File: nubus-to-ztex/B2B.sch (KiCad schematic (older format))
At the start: 13 parts, among them J1 87832-1420 (2x7 M 2mm), J3 Conn_01x06_Male

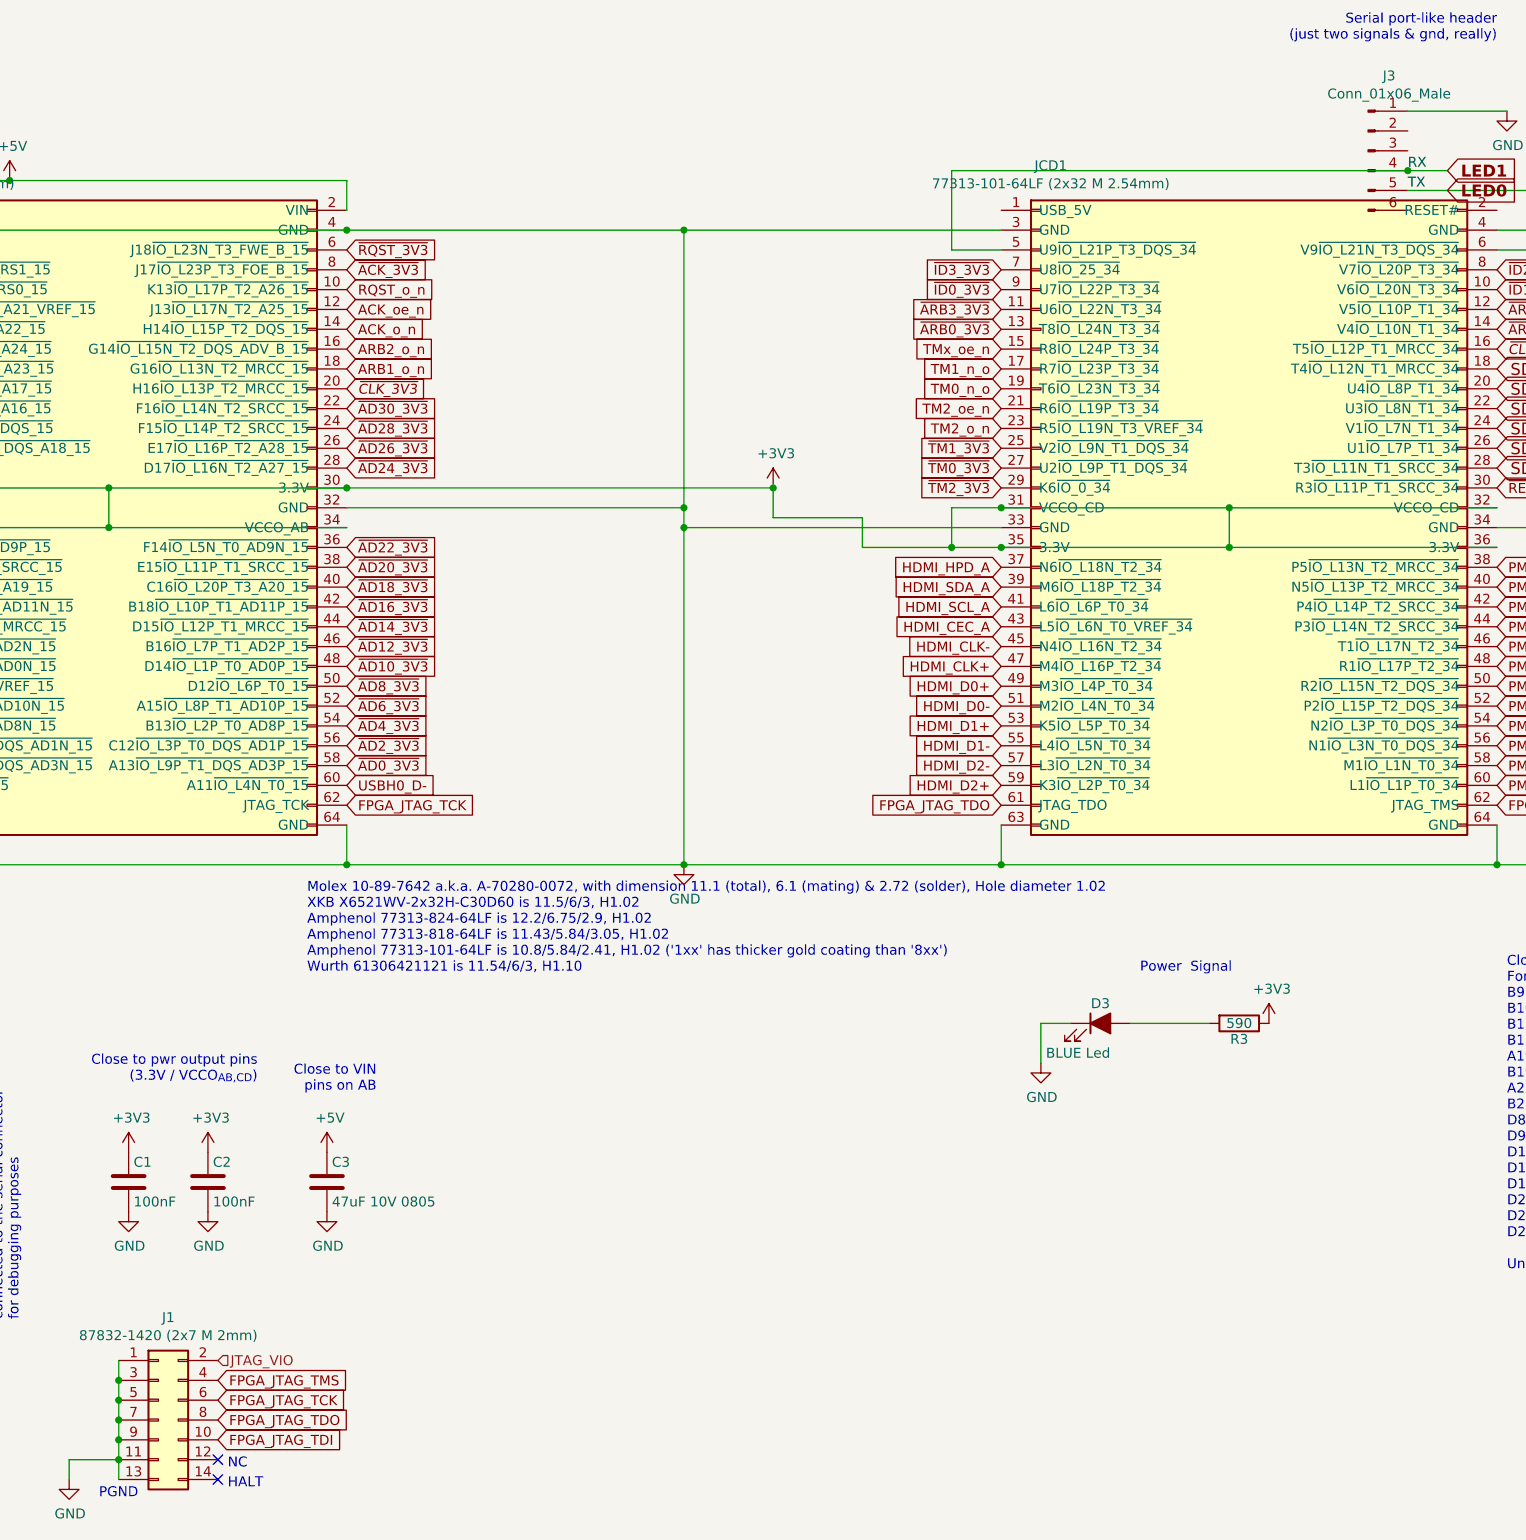
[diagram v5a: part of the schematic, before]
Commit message: more THT->SMT, lexx expensive parts/assembly (?)
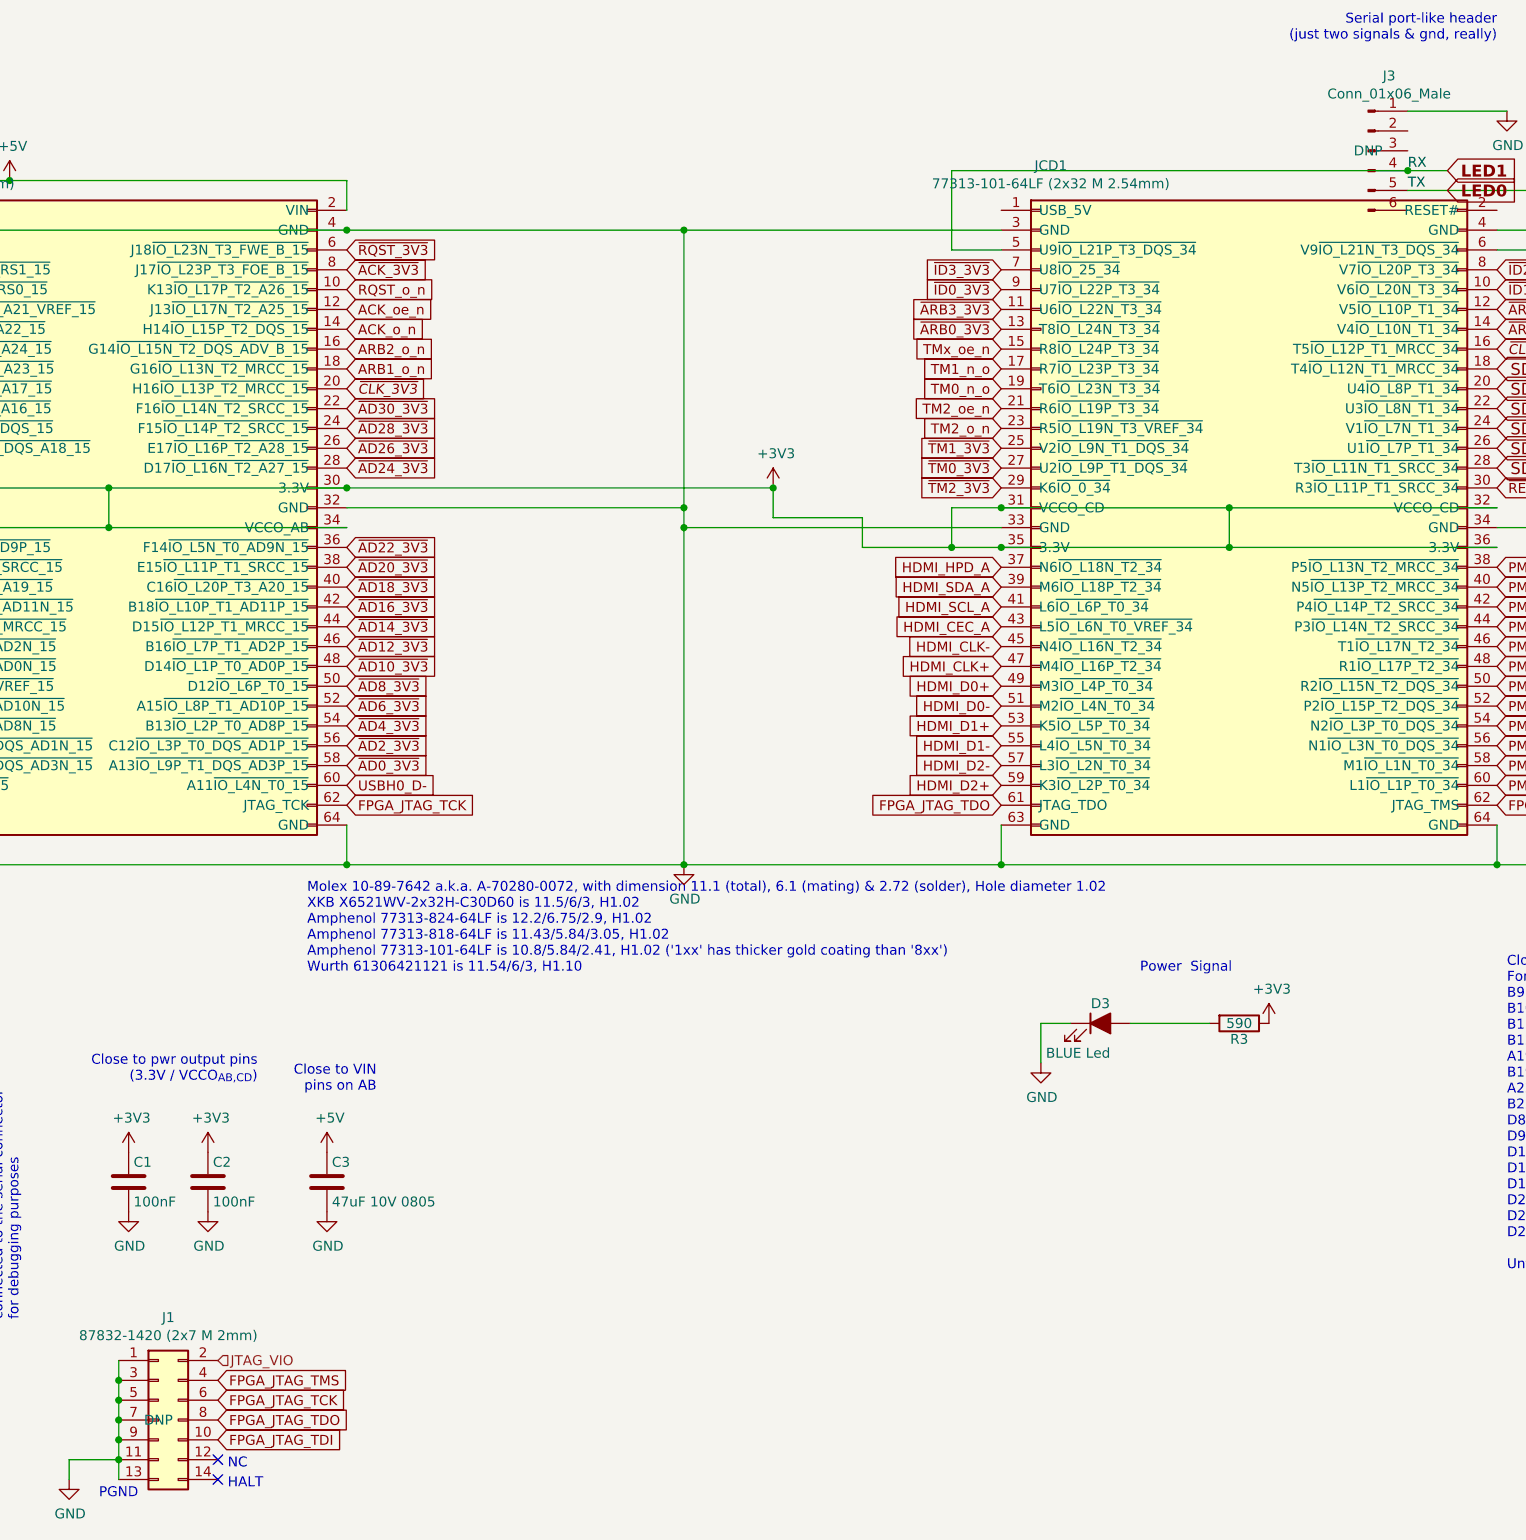
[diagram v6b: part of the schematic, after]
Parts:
- J1: DNP (none) -> DNP
- J3: footprint For_SeeedStudio:PinHeader_1x06_P2.54mm_Horizontal_For_SeeedStudio -> For_SeeedStudio:SAMTEC_TSM-106-01-L-SH; DNP (none) -> DNP; MPN PZ254R-11-06P -> TSM-106-01-T-SH; MPN comments (none) -> 'T' is tin 'L' is gold ; with extra -A (and footprint chang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; MPN-ALT 22-28-8060 -> (none); URL https://lcsc.com/product-detail/Pin-Header-Female-Header_XF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 -> https://www.mouser.fr/ProductDetail/Samtec/TSM-106-01-T-SH?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; URL-ALT https://www2.mouser.com/ProductDetail/Molex/22-28-8060?qs=4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 -> (none)
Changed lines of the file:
@@
 F 0 "J3" H 9356 1228 50  0000 C CNN
 F 1 "Conn_01x06_Male" H 9356 1137 50  0000 C CNN
-F 2 "For_SeeedStudio:PinHeader_1x06_P2.54mm_Horizontal_For_SeeedStudio" H 9250 850 50  0001 C CNN
-F 3 "~" H 9250 850 50  0001 C CNN
-F 4 "22-28-8060" H 9250 850 50  0001 C CNN "MPN-ALT"
-F 5 "PZ254R-11-06P" H 9250 850 50  0001 C CNN "MPN"
-F 6 "https://www2.mouser.com/ProductDetail/Molex/22-28-8060?qs=4XSMV6Twtb2rYD%2F%2F316gfQ==" H 9250 850 50  0001 C CNN "URL-ALT"
-F 7 "https://lcsc.com/product-detail/Pin-Header-Female-Header_XFCN-PZ254R-11-06P_C492414.html" H 9250 850 50  0001 C CNN "URL"
+F 2 "For_SeeedStudio:SAMTEC_TSM-106-01-L-SH" H 9250 850 50  0001 C CNN
+F 3 "https://www.mouser.com/datasheet/2/527/tsm-2854655.pdf" H 9250 850 50  0001 C CNN
+F 4 "TSM-106-01-T-SH" H 9250 850 50  0001 C CNN "MPN"
+F 5 "https://www.mouser.fr/ProductDetail/Samtec/TSM-106-01-T-SH?qs=0lQeLiL1qybjt4R2%252BGOpsA%3D%3D" H 9250 850 50  0001 C CNN "URL"
+F 6 "'T' is tin 'L' is gold ; with extra -A (and footprint change) to get alignment pin ; -01 is post length (-02 would be fine)" H 9250 850 50  0001 C CNN "MPN comments"
+F 7 "DNP" H 9250 850 50  0000 C CNN "DNP"
 	1    9250 850
 	1    0    0    -1
@@
 F 4 "87832-1420" H 3150 7250 50  0001 C CNN "MPN"
 F 5 "https://www.mouser.fr/ProductDetail/Molex/87832-1420?qs=9Wl4wMk6Njp2JciwISLQUQ%3D%3D" H 3150 7250 50  0001 C CNN "URL"
+F 6 "DNP" H 3150 7250 50  0000 C CNN "DNP"
 	1    3150 7250
 	1    0    0    -1

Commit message: minor cleanups
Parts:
- C1, C2: LCSC ? -> (none)
- D1, D2: value RED Led -> RED Led 0805
- D3: value BLUE Led -> BLUE Led 0805
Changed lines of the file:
@@
 AR Path="/618E8C75/61B5DFCC" Ref="D1"  Part="1"
 F 0 "D1" H 1000 6000 50  0000 C CNN
-F 1 "RED Led" H 1050 5750 50  0000 R CNN
+F 1 "RED Led 0805" H 1050 5750 50  0000 R CNN
 F 2 "LED_SMD:LED_0805_2012Metric" H 1000 5900 50  0001 C CNN
 F 3 "https://optoelectronics.liteon.com/upload/download/DS-22-99-0150/LTST-C170KRKT.pdf" H 1000 5900 50  0001 C CNN
@@
 AR Path="/618E8C75/61B5F405" Ref="D2"  Part="1"
 F 0 "D2" H 1000 6500 50  0000 C CNN
-F 1 "RED Led" H 1050 6250 50  0000 R CNN
+F 1 "RED Led 0805" H 1050 6250 50  0000 R CNN
 F 2 "LED_SMD:LED_0805_2012Metric" H 1000 6400 50  0001 C CNN
 F 3 "https://optoelectronics.liteon.com/upload/download/DS-22-99-0150/LTST-C170KRKT.pdf" H 1000 6400 50  0001 C CNN
@@
 F 6 "603-CC603KRX7R8BB104" H 3000 6050 50  0001 C CNN "Mouser"
 F 7 "?" H 3000 6050 50  0001 C CNN "Digikey"
-F 8 "?" H 3000 6050 50  0001 C CNN "LCSC"
+F 8 "" H 3000 6050 50  0001 C CNN "LCSC"
 F 9 "?" H 3000 6050 50  0001 C CNN "Koncar"
 F 10 "TB" H 3000 6050 50  0001 C CNN "Side"
@@
 F 6 "603-CC603KRX7R8BB104" H 3400 6050 50  0001 C CNN "Mouser"
 F 7 "?" H 3400 6050 50  0001 C CNN "Digikey"
-F 8 "?" H 3400 6050 50  0001 C CNN "LCSC"
+F 8 "" H 3400 6050 50  0001 C CNN "LCSC"
 F 9 "?" H 3400 6050 50  0001 C CNN "Koncar"
 F 10 "TB" H 3400 6050 50  0001 C CNN "Side"
@@
 AR Path="/618E8C75/621E3C57" Ref="D3"  Part="1"
 F 0 "D3" H 7900 5350 50  0000 C CNN
-F 1 "BLUE Led" H 7950 5100 50  0000 R CNN
+F 1 "BLUE Led 0805" H 7950 5100 50  0000 R CNN
 F 2 "LED_SMD:LED_0805_2012Metric" H 7900 5250 50  0001 C CNN
 F 3 "https://eu.mouser.com/datasheet/2/239/Lite-On-LTST-C170TBKT-1175372.pdf" H 7900 5250 50  0001 C CNN
